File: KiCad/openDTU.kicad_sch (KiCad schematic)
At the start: 25 parts, among them J1 USB_C_Receptacle_USB2.0, J2 Conn_Coaxial, U3 ESP32-WROOM-32, U4 nRF24L01P, U5 NCP1117-3.3_SOT223, Y1 Crystal

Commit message: adding 3D Model for USB-C connector
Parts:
- C11, C12: footprint Capacitor_Tantalum_SMD:CP_EIA-1608-10_AVX-L -> Capacitor_SMD:C_1210_3225Metric_Pad1.33x2.70mm_HandSolder
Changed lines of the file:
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@@
       (effects (font (size 1.27 1.27)) (justify left))
     )
-    (property "Footprint" "Capacitor_Tantalum_SMD:CP_EIA-1608-10_AVX-L" (id 2) (at 147.066 188.087 0)
+    (property "Footprint" "Capacitor_SMD:C_1210_3225Metric_Pad1.33x2.70mm_HandSolder" (id 2) (at 147.066 188.087 0)
       (effects (font (size 1.27 1.27)) hide)
     )
@@
       (effects (font (size 1.27 1.27)) (justify left))
     )
-    (property "Footprint" "Capacitor_Tantalum_SMD:CP_EIA-1608-10_AVX-L" (id 2) (at 119.634 188.214 0)
+    (property "Footprint" "Capacitor_SMD:C_1210_3225Metric_Pad1.33x2.70mm_HandSolder" (id 2) (at 119.634 188.214 0)
       (effects (font (size 1.27 1.27)) hide)
     )
@@
     )
     (path "/988a5f1f-a1c1-458a-a00b-6b951a8d2dbc"
-      (reference "C11") (unit 1) (value "10uF") (footprint "Capacitor_Tantalum_SMD:CP_EIA-1608-10_AVX-L")
+      (reference "C11") (unit 1) (value "10uF") (footprint "Capacitor_SMD:C_1210_3225Metric_Pad1.33x2.70mm_HandSolder")
     )
     (path "/b1904461-1850-4a3b-952c-b4406bca6c6d"
-      (reference "C12") (unit 1) (value "10uF") (footprint "Capacitor_Tantalum_SMD:CP_EIA-1608-10_AVX-L")
+      (reference "C12") (unit 1) (value "10uF") (footprint "Capacitor_SMD:C_1210_3225Metric_Pad1.33x2.70mm_HandSolder")
     )
     (path "/812aa465-9699-4cfc-9d0c-8b6dbbe2e097"

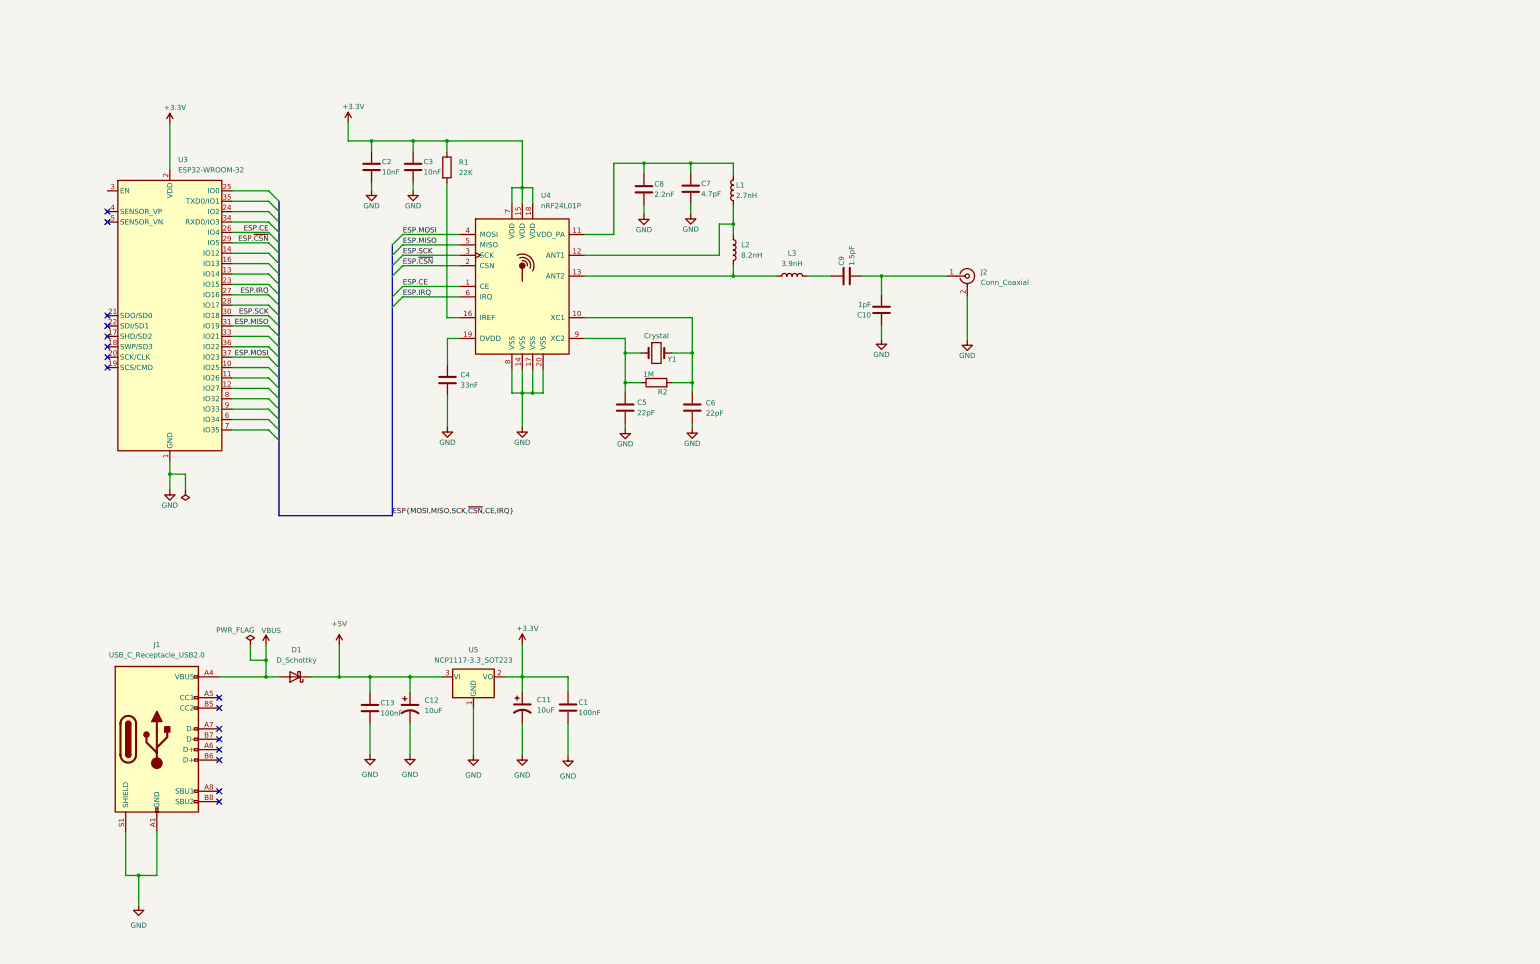
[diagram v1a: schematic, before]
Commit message: adding microSD socket and reset switch to schematic
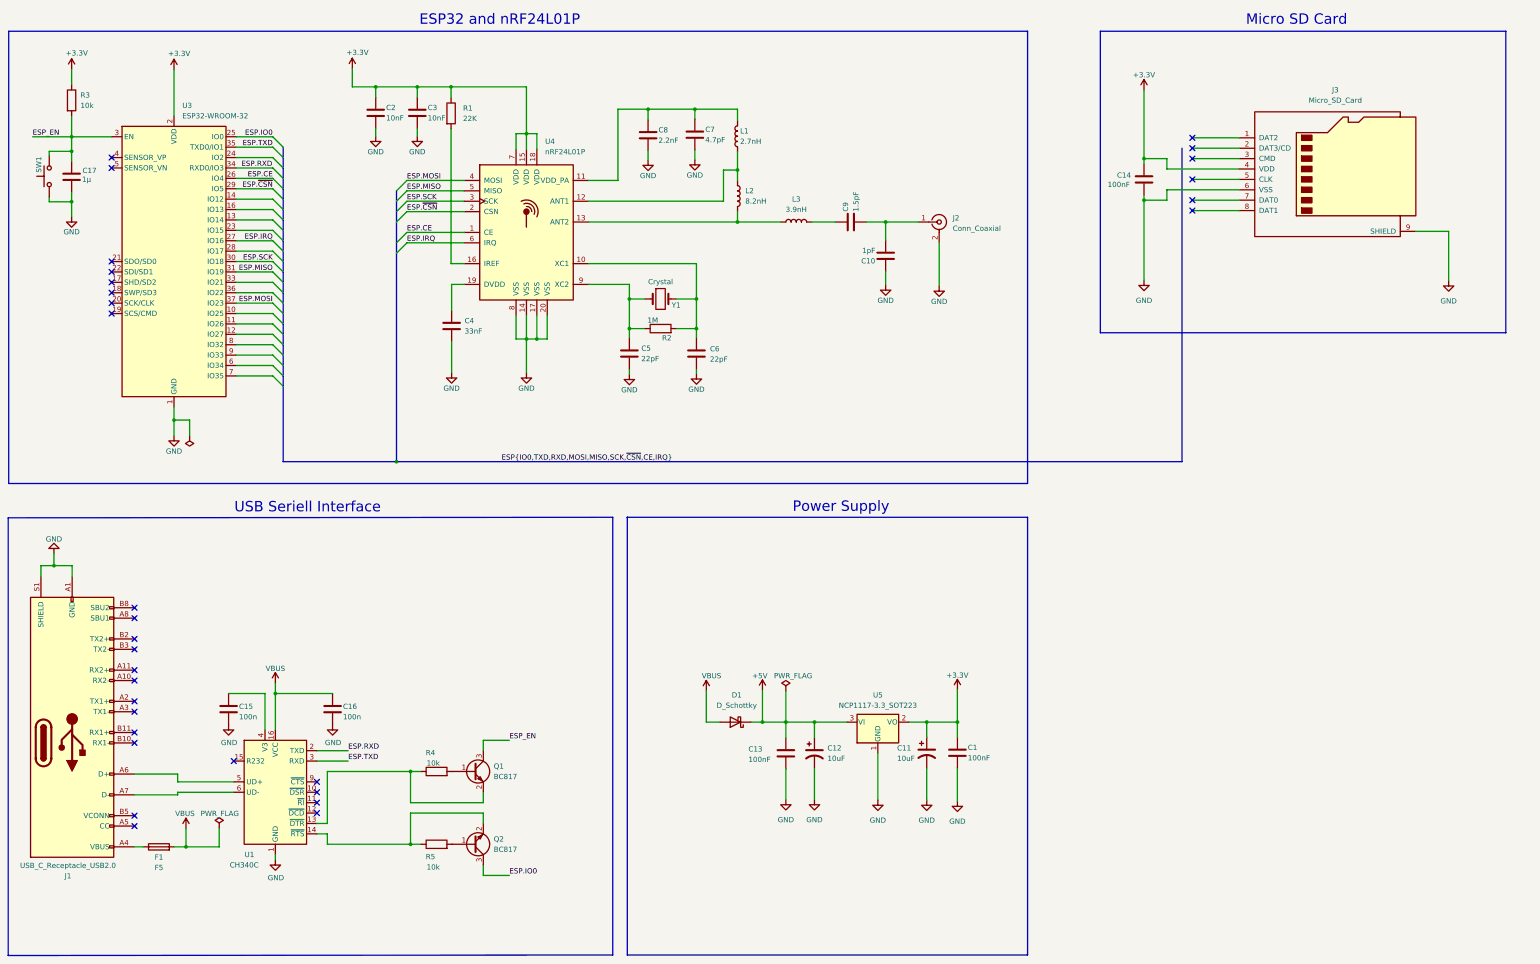
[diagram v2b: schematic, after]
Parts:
- added C14: 100nF, Capacitor_SMD:C_0603_1608Metric_Pad1.08x0.95mm_HandSolder, symbol Device:C
- added C15, C16: 100n, Capacitor_SMD:C_0603_1608Metric, symbol Device:C
- added C17: 1µ, Capacitor_SMD:C_0603_1608Metric, symbol Device:C
- added F1: F5, Fuse:Fuse_Littelfuse-NANO2-451_453, symbol Device:Fuse
- added J3: Micro_SD_Card, Connector_Card:microSD_HC_Hirose_DM3AT-SF-PEJM5, symbol Connector:Micro_SD_Card
- added Q1, Q2: BC817, Package_TO_SOT_SMD:SOT-23, symbol Transistor_BJT:BC817
- added R3: 10k, Resistor_SMD:R_0603_1608Metric_Pad0.98x0.95mm_HandSolder, symbol Device:R
- added R4, R5: 10k, Resistor_SMD:R_0603_1608Metric, symbol Device:R
- added SW1: SW_Push, Button_Switch_SMD:SW_SPST_B3U-1000P, symbol Switch:SW_Push
- added U1: CH340C, Package_SO:SOIC-16_3.9x9.9mm_P1.27mm, symbol Interface_USB:CH340C
- J1: symbol Connector:USB_C_Receptacle_USB2.0 -> Connector:USB_C_Plug
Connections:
- net +3.3V: now also C14.1, J3.4 (VDD), R3.1
- net GND: now also C14.2, C15.2, C16.2, C17.2, J3.6 (VSS), J3.9 (SHIELD), SW1.1, U1.1 (GND)
- net VBUS: now also C16.1, F1.2, U1.16 (VCC); no longer J1.A4 (VBUS), J1.A9 (VBUS), J1.B4 (VBUS), J1.B9 (VBUS)
- net ESP.IO0: now reaches U3.25 (IO0)
- net ESP.IO0: now also Q2.3 (C)
- net ESP_EN: now reaches U3.3 (EN)
- net ESP_EN: now also C17.1, Q1.3 (C), R3.2, SW1.2
- net ESP.RXD: now reaches U3.34 (RXD0/IO3)
- net ESP.RXD: now also U1.2 (TXD)
- net ESP.TXD: now reaches U3.35 (TXD0/IO1)
- net ESP.TXD: now also U1.3 (RXD)
- net at J1.A6 (D+): now also U1.5 (UD+)
- net at J1.A7 (D-): now also U1.6 (UD-)
- new net: Q2.2 (E), R5.1, U1.14 (~{RTS})
- new net: Q2.1 (B), R5.2
- new net: Q1.1 (B), R4.2
- new net: Q1.2 (E), R4.1, U1.13 (~{DTR})
- new net: C15.1, U1.4 (V3)
- new net: F1.1, J1.A4 (VBUS), J1.A9 (VBUS), J1.B4 (VBUS), J1.B9 (VBUS)
- no-connect marks 16 -> 31
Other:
- note added: "ESP32 and nRF24L01P"
- note added: "Micro SD Card"
- note added: "Power Supply"
- note added: "USB Seriell Interface"
- moved on the sheet: C1, C10, C11, C12, C13, C2, C3, C4, C5, C6, C7, C8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

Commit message: adding BOOT switch buttom
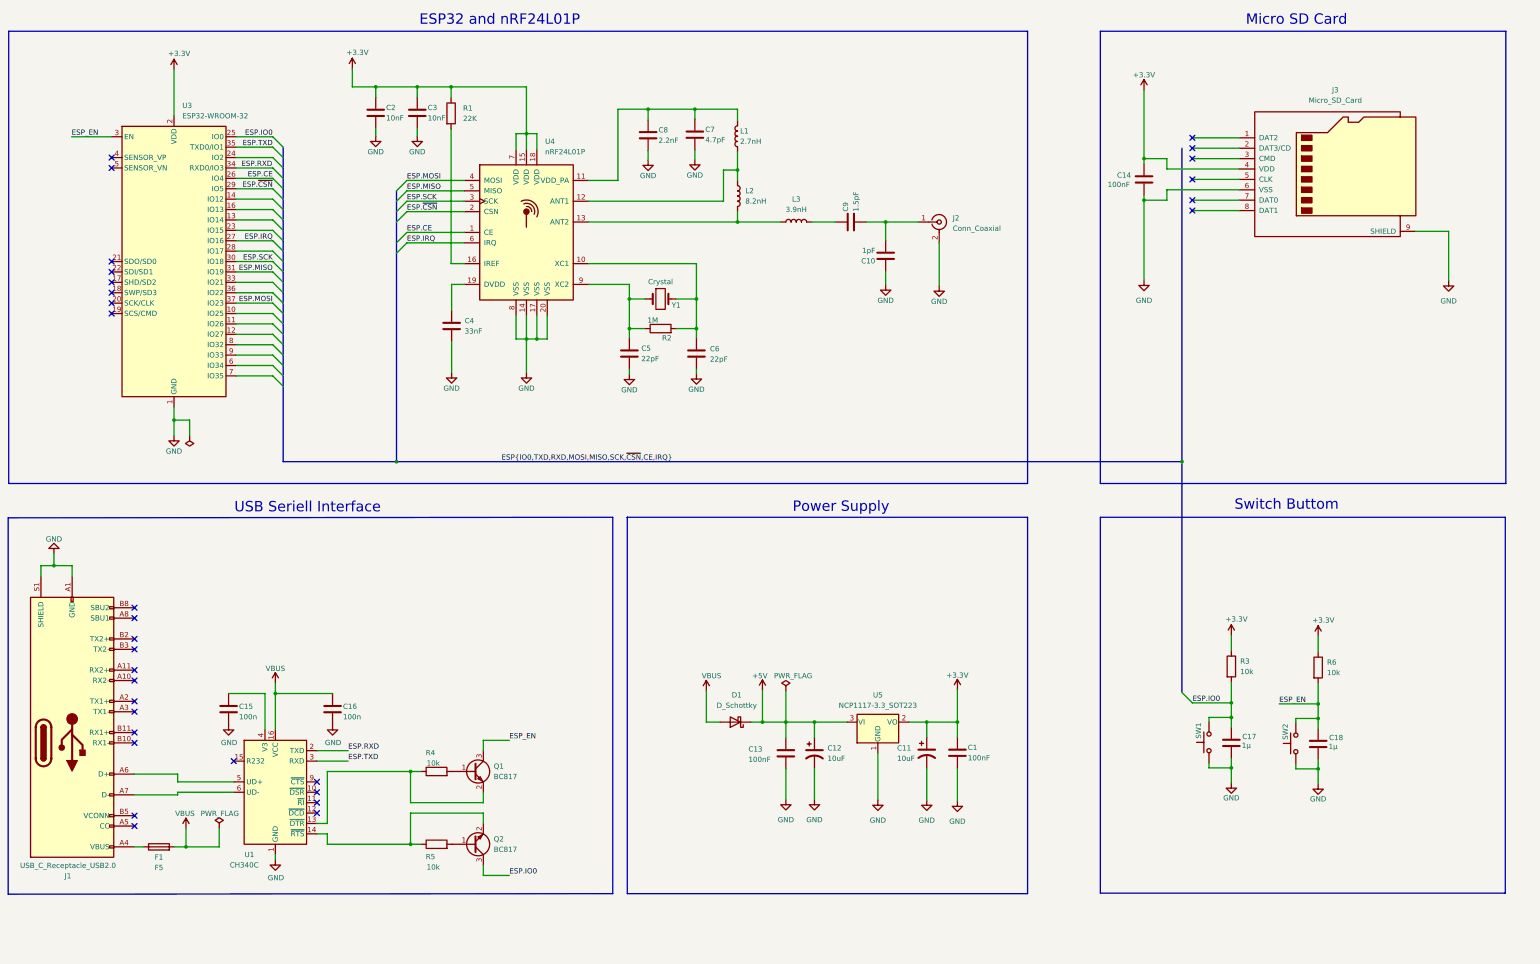
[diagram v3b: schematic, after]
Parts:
- added C18: 1µ, Capacitor_SMD:C_0603_1608Metric, symbol Device:C
- added R6: 10k, Resistor_SMD:R_0603_1608Metric_Pad0.98x0.95mm_HandSolder, symbol Device:R
- added SW2: SW_Push, Button_Switch_SMD:SW_SPST_B3U-1000P, symbol Switch:SW_Push
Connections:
- net +3.3V: now also R6.1
- net ESP.IO0: now also C17.1, R3.2, SW1.2
- net ESP_EN: now also C18.1, R6.2, SW2.2; no longer C17.1, R3.2, SW1.2
- net GND: now also C18.2, SW2.1
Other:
- note added: "Switch Buttom"

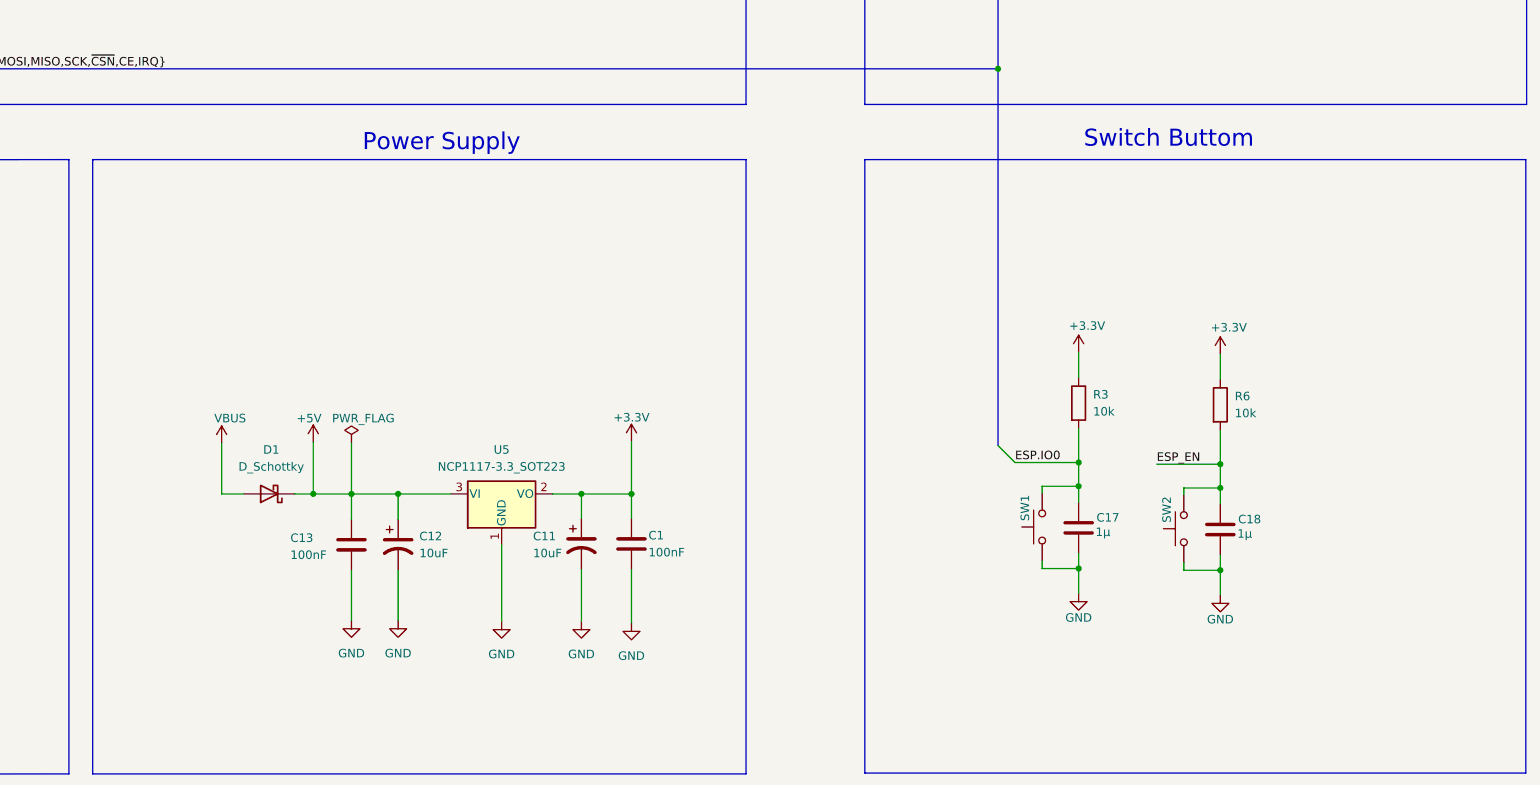
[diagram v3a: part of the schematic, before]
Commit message: adding User (GPIO1) and Power LED
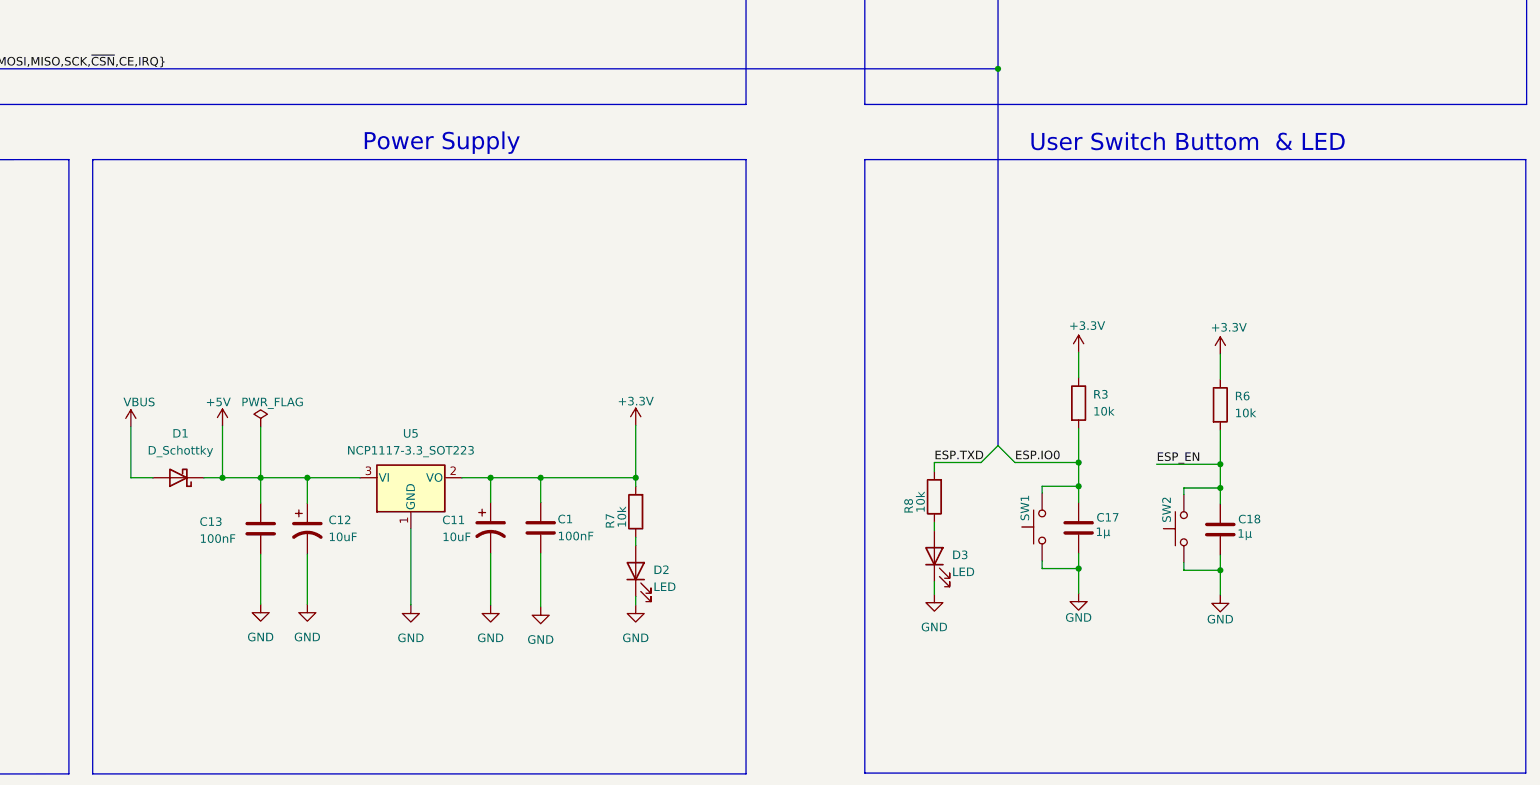
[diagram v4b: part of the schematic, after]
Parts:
- added D2, D3: LED, LED_SMD:LED_0603_1608Metric_Pad1.05x0.95mm_HandSolder, symbol Device:LED
- added R7, R8: 10k, Resistor_SMD:R_0603_1608Metric, symbol Device:R
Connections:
- net +3.3V: now also R7.2
- net ESP.TXD: now also R8.2
- net GND: now also D2.1 (K), D3.1 (K)
- new net: D2.2 (A), R7.1
- new net: D3.2 (A), R8.1
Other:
- note added: "User Switch Buttom & LED"
- note removed: "Switch Buttom"
- moved on the sheet: C1, C11, C12, C13, D1, U5
